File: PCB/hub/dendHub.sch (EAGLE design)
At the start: 12 parts

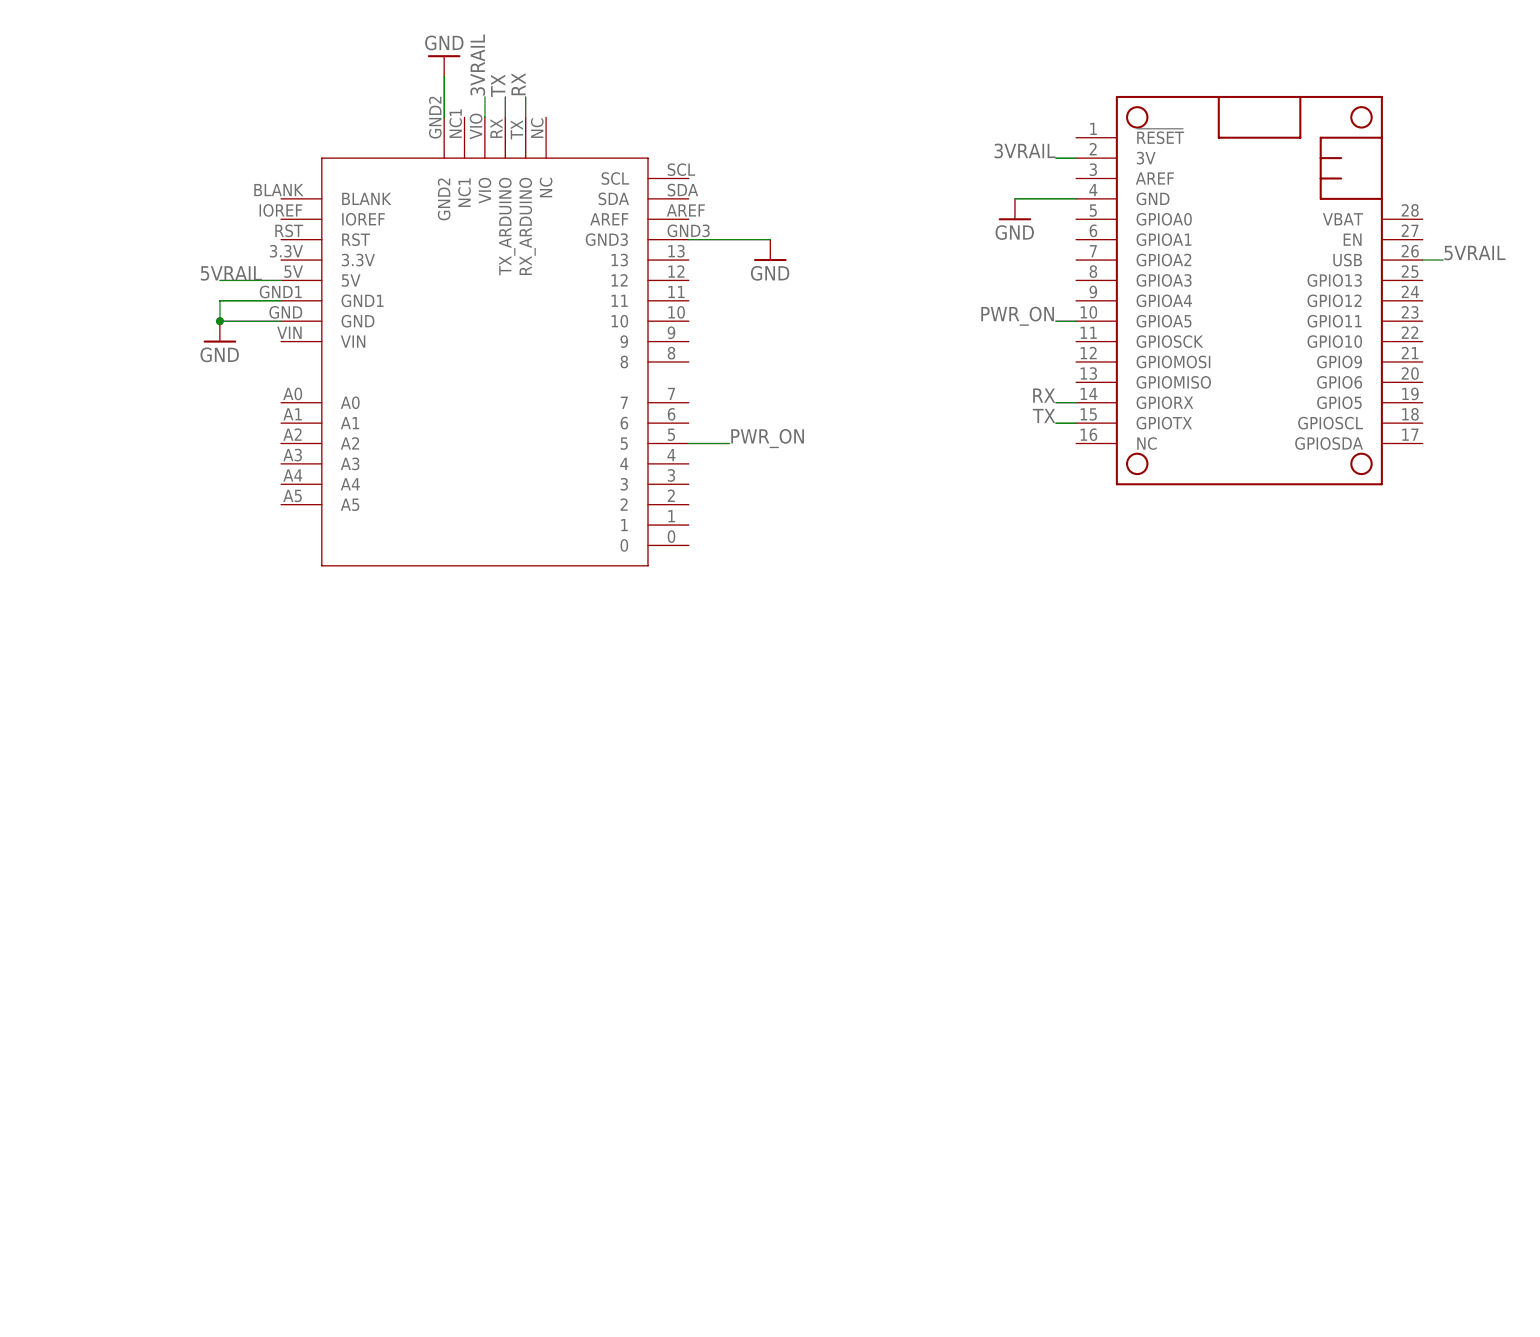
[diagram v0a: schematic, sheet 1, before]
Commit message: Summer 2022 Deployment Prep
Updated PCBs and code, includes Loom V3 and HypnosV3.3 changes
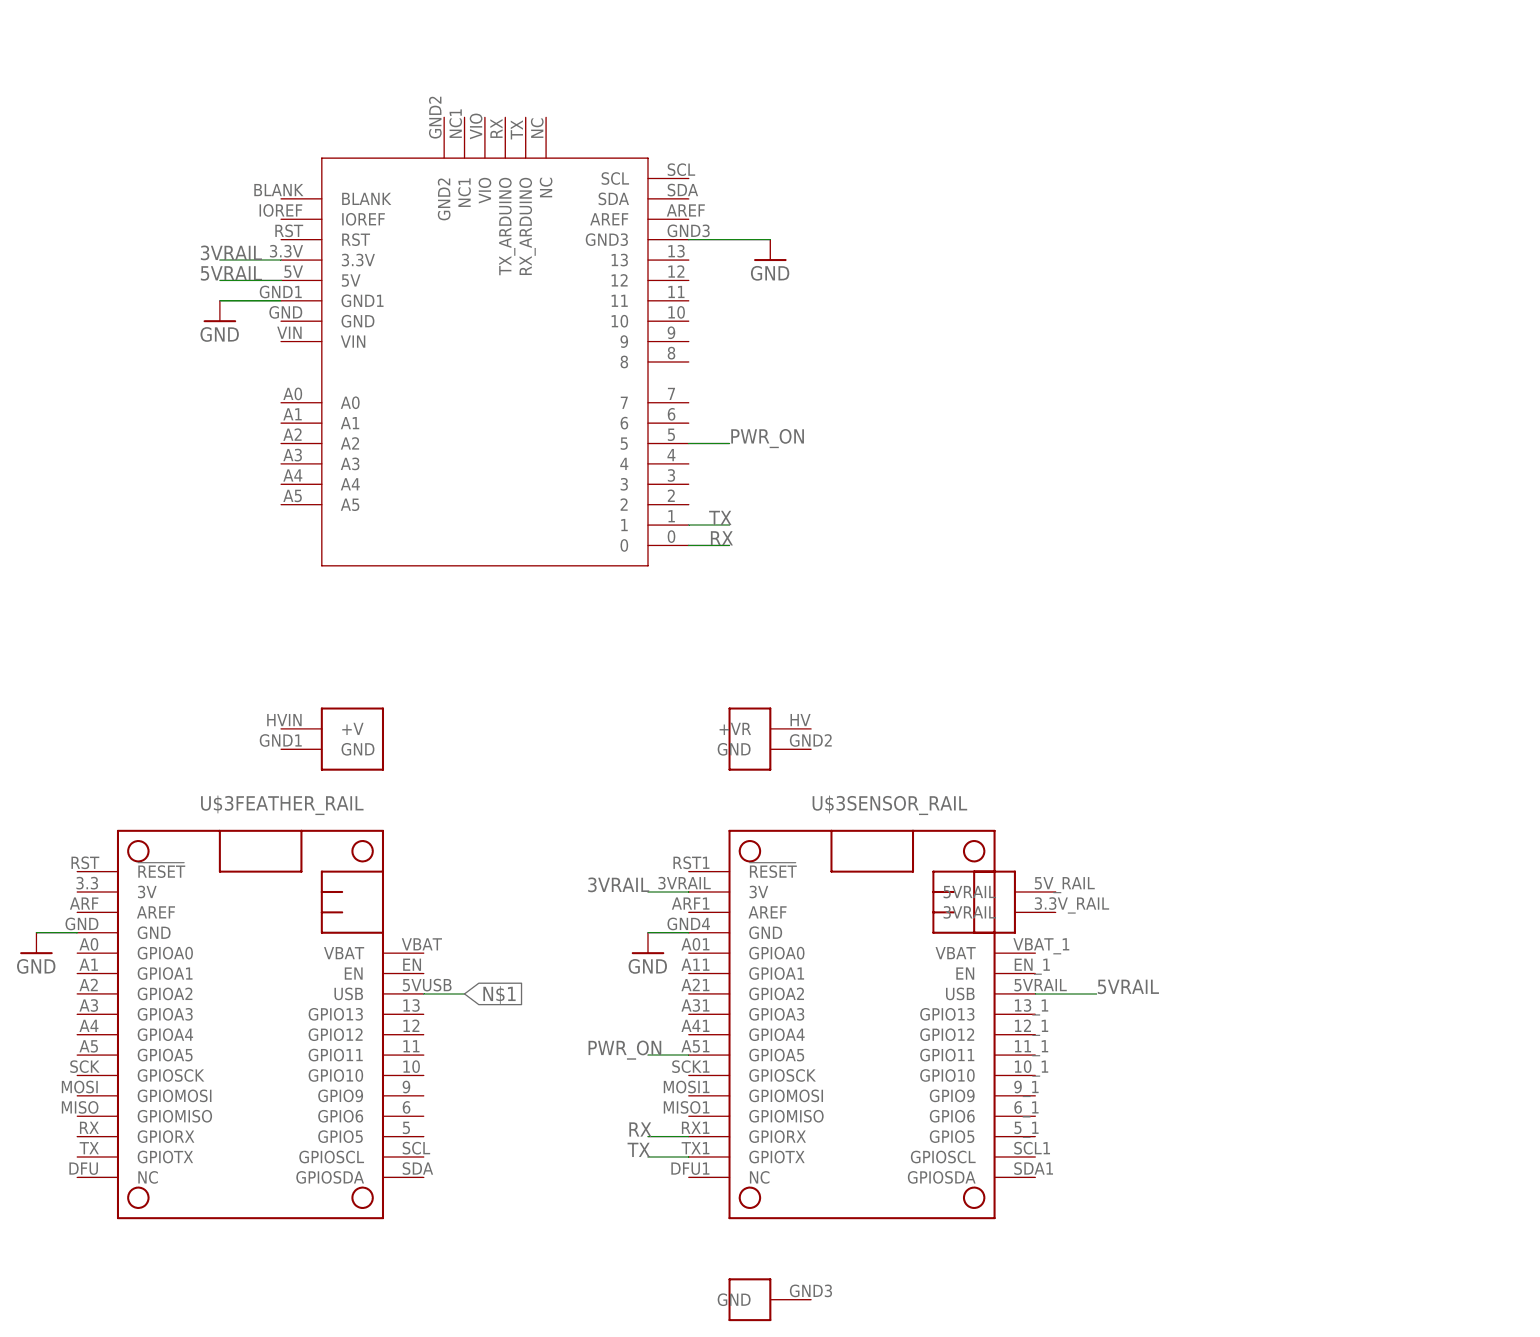
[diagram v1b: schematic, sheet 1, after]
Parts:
- removed MS1: FEATHERWING, adafruit:FEATHERWING
- added U$3: HYPNOS_V3, HYPNOS_V3:HYPNOS_V3
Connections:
- net 3VRAIL: now also U$1.3.3V, U$3SENSOR_RAIL.3V; no longer MS1.3V, U$1.VIO
- net 5VRAIL: now also U$3SENSOR_RAIL.USB; no longer MS1.USB
- net GND: now also U$3FEATHER_RAIL.GND, U$3SENSOR_RAIL.GND; no longer MS1.GND, U$1.GND, U$1.GND2
- net N$1: now also U$3FEATHER_RAIL.USB
- net PWR_ON: now also U$3SENSOR_RAIL.GPIOA5; no longer MS1.GPIOA5
- net RX: now also U$1.0, U$3SENSOR_RAIL.GPIORX; no longer MS1.GPIORX, U$1.RX_ARDUINO
- net TX: now also U$1.1, U$3SENSOR_RAIL.GPIOTX; no longer MS1.GPIOTX, U$1.TX_ARDUINO
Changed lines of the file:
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@@
 <groups>
 <schematic_group name="LTE_BOARD"/>
-<schematic_group name="FEATHER"/>
 <schematic_group name="SOLARCHARGER"/>
 <schematic_group name="POWERBOOSTER"/>
+<schematic_group name="FEATHER/HYPNOS"/>
 </groups>
 <parts>
-<part name="GND1" library="supply1" library_urn="urn:adsk.eagle:library:371" deviceset="GND" device=""/>
-<part name="MS1" library="adafruit" deviceset="FEATHERWING" device="" package3d_urn="urn:adsk.eagle:package:6240959/1"/>
 <part name="U$1" library="LTE_BOARD" deviceset="LTE_BOARD" device=""/>
-<part name="GND5" library="supply1" library_urn="urn:adsk.eagle:library:371" deviceset="GND" device=""/>
 <part name="GND9" library="supply1" library_urn="urn:adsk.eagle:library:371" deviceset="GND" device=""/>
 <part name="GND6" library="supply1" library_urn="urn:adsk.eagle:library:371" deviceset="GND" device=""/>
@@
 <part name="U$83" library="microbuilder" deviceset="GND" device=""/>
 <part name="JP1" library="microbuilder" deviceset="HEADER-1X8" device="ROUND"/>
+<part name="U$3" library="HYPNOS_V3" deviceset="HYPNOS_V3" device="" package3d_urn="urn:adsk.eagle:package:28031607/1"/>
+<part name="GND2" library="supply1" library_urn="urn:adsk.eagle:library:371" deviceset="GND" device=""/>
+<part name="GND3" library="supply1" library_urn="urn:adsk.eagle:library:371" deviceset="GND" device=""/>
 </parts>
 <sheets>
@@
 </plain>
 <instances>
-<instance part="GND1" gate="1" x="-81.28" y="198.12" smashed="yes" grouprefs="FEATHER">
-<attribute name="VALUE" x="-83.82" y="195.58" size="1.778" layer="96"/>
-</instance>
-<instance part="MS1" gate="G$1" x="-68.58" y="213.36" smashed="yes" rot="R270" grouprefs="FEATHER"/>
 <instance part="U$1" gate="G$1" x="-157.48" y="177.8" smashed="yes" grouprefs="LTE_BOARD"/>
-<instance part="GND5" gate="1" x="-152.4" y="218.44" smashed="yes" rot="R180" grouprefs="LTE_BOARD">
-<attribute name="VALUE" x="-149.86" y="220.98" size="1.778" layer="96" rot="R180"/>
-</instance>
 <instance part="GND9" gate="1" x="-111.76" y="193.04" smashed="yes" grouprefs="LTE_BOARD">
 <attribute name="VALUE" x="-114.3" y="190.5" size="1.778" layer="96"/>
 </instance>
-<instance part="GND6" gate="1" x="-180.34" y="182.88" smashed="yes" grouprefs="LTE_BOARD">
-<attribute name="VALUE" x="-182.88" y="180.34" size="1.778" layer="96"/>
+<instance part="GND6" gate="1" x="-180.34" y="185.42" smashed="yes" grouprefs="LTE_BOARD">
+<attribute name="VALUE" x="-182.88" y="182.88" size="1.778" layer="96"/>
+</instance>
+<instance part="U$3" gate="FEATHER_RAIL" x="-195.58" y="81.28" smashed="yes" grouprefs="FEATHER/HYPNOS">
+<attribute name="NAME" x="-182.88" y="124.46" size="1.778" layer="95"/>
+</instance>
+<instance part="U$3" gate="SENSOR_RAIL" x="-119.38" y="81.28" smashed="yes" grouprefs="FEATHER/HYPNOS">
+<attribute name="NAME" x="-106.68" y="124.46" size="1.778" layer="95"/>
+</instance>
+<instance part="U$3" gate="G$1" x="-215.9" y="91.44" smashed="yes" grouprefs="FEATHER/HYPNOS"/>
+<instance part="U$3" gate="G$2" x="-114.3" y="132.08" smashed="yes" grouprefs="FEATHER/HYPNOS"/>
+<instance part="U$3" gate="G$3" x="-114.3" y="63.5" smashed="yes" grouprefs="FEATHER/HYPNOS"/>
+<instance part="U$3" gate="G$4" x="-83.82" y="111.76" smashed="yes" grouprefs="FEATHER/HYPNOS"/>
+<instance part="GND2" gate="1" x="-203.2" y="106.68" smashed="yes" grouprefs="FEATHER/HYPNOS">
+<attribute name="VALUE" x="-205.74" y="104.14" size="1.778" layer="96"/>
+</instance>
+<instance part="GND3" gate="1" x="-127" y="106.68" smashed="yes" grouprefs="FEATHER/HYPNOS">
+<attribute name="VALUE" x="-129.54" y="104.14" size="1.778" layer="96"/>
 </instance>
 </instances>
@@
 <nets>
 <net name="GND" class="0">
-<segment>
-<pinref part="GND1" gate="1" pin="GND"/>
-<wire x1="-81.28" y1="200.66" x2="-73.66" y2="200.66" width="0.1524" layer="91" grouprefs="FEATHER"/>
-<pinref part="MS1" gate="G$1" pin="GND"/>
-</segment>
-<segment>
-<wire x1="-152.4" y1="210.82" x2="-152.4" y2="215.9" width="0.1524" layer="91" grouprefs="LTE_BOARD"/>
-<pinref part="U$1" gate="G$1" pin="GND2"/>
-<pinref part="GND5" gate="1" pin="GND"/>
-</segment>
 <segment>
 <pinref part="U$1" gate="G$1" pin="GND3"/>
@@
 <pinref part="U$1" gate="G$1" pin="GND1"/>
 <wire x1="-172.72" y1="187.96" x2="-180.34" y2="187.96" width="0.1524" layer="91" grouprefs="LTE_BOARD"/>
-<wire x1="-180.34" y1="187.96" x2="-180.34" y2="185.42" width="0.1524" layer="91" grouprefs="LTE_BOARD"/>
-<pinref part="U$1" gate="G$1" pin="GND"/>
-<wire x1="-180.34" y1="185.42" x2="-172.72" y2="185.42" width="0.1524" layer="91" grouprefs="LTE_BOARD"/>
 <pinref part="GND6" gate="1" pin="GND"/>
-<junction x="-180.34" y="185.42" grouprefs="LTE_BOARD"/>
+</segment>
+<segment>
+<pinref part="U$3" gate="FEATHER_RAIL" pin="GND"/>
+<wire x1="-198.12" y1="109.22" x2="-203.2" y2="109.22" width="0.1524" layer="91" grouprefs="FEATHER/HYPNOS"/>
+<pinref part="GND2" gate="1" pin="GND"/>
+</segment>
+<segment>
+<pinref part="U$3" gate="SENSOR_RAIL" pin="GND"/>
+<wire x1="-121.92" y1="109.22" x2="-127" y2="109.22" width="0.1524" layer="91" grouprefs="FEATHER/HYPNOS"/>
+<pinref part="GND3" gate="1" pin="GND"/>
 </segment>
 </net>
 <net name="TX" class="0">
 <segment>
-<wire x1="-73.66" y1="172.72" x2="-76.2" y2="172.72" width="0.1524" layer="91" grouprefs="FEATHER"/>
-<label x="-76.2" y="172.72" size="1.778" layer="95" rot="MR0" grouprefs="FEATHER"/>
-<pinref part="MS1" gate="G$1" pin="GPIOTX"/>
+<pinref part="U$1" gate="G$1" pin="1"/>
+<wire x1="-121.92" y1="160.02" x2="-116.84" y2="160.02" width="0.1524" layer="91"/>
+<label x="-119.38" y="160.02" size="1.778" layer="95"/>
 </segment>
 <segment>
-<wire x1="-144.78" y1="210.82" x2="-144.78" y2="213.36" width="0.1524" layer="91" grouprefs="LTE_BOARD"/>
-<label x="-144.78" y="213.36" size="1.778" layer="95" rot="R90" grouprefs="LTE_BOARD"/>
-<pinref part="U$1" gate="G$1" pin="TX_ARDUINO"/>
+<pinref part="U$3" gate="SENSOR_RAIL" pin="GPIOTX"/>
+<wire x1="-121.92" y1="81.28" x2="-127" y2="81.28" width="0.1524" layer="91" grouprefs="FEATHER/HYPNOS"/>
+<label x="-129.54" y="81.28" size="1.778" layer="95" grouprefs="FEATHER/HYPNOS"/>
 </segment>
 </net>
 <net name="RX" class="0">
 <segment>
-<wire x1="-73.66" y1="175.26" x2="-76.2" y2="175.26" width="0.1524" layer="91" grouprefs="FEATHER"/>
-<label x="-76.2" y="175.26" size="1.778" layer="95" rot="MR0" grouprefs="FEATHER"/>
-<pinref part="MS1" gate="G$1" pin="GPIORX"/>
+<pinref part="U$1" gate="G$1" pin="0"/>
+<wire x1="-121.92" y1="157.48" x2="-116.84" y2="157.48" width="0.1524" layer="91"/>
+<label x="-119.38" y="157.48" size="1.778" layer="95"/>
 </segment>
 <segment>
-<wire x1="-142.24" y1="210.82" x2="-142.24" y2="213.36" width="0.1524" layer="91" grouprefs="LTE_BOARD"/>
-<label x="-142.24" y="213.36" size="1.778" layer="95" rot="R90" grouprefs="LTE_BOARD"/>
-<pinref part="U$1" gate="G$1" pin="RX_ARDUINO"/>
+<pinref part="U$3" gate="SENSOR_RAIL" pin="GPIORX"/>
+<wire x1="-121.92" y1="83.82" x2="-127" y2="83.82" width="0.1524" layer="91" grouprefs="FEATHER/HYPNOS"/>
+<label x="-129.54" y="83.82" size="1.778" layer="95" grouprefs="FEATHER/HYPNOS"/>
 </segment>
 </net>
@@
 </segment>
 <segment>
-<wire x1="-73.66" y1="185.42" x2="-76.2" y2="185.42" width="0.1524" layer="91" grouprefs="FEATHER"/>
-<label x="-76.2" y="185.42" size="1.778" layer="95" rot="MR0" grouprefs="FEATHER"/>
-<pinref part="MS1" gate="G$1" pin="GPIOA5"/>
+<pinref part="U$3" gate="SENSOR_RAIL" pin="GPIOA5"/>
+<wire x1="-121.92" y1="93.98" x2="-127" y2="93.98" width="0.1524" layer="91" grouprefs="FEATHER/HYPNOS"/>
+<label x="-134.62" y="93.98" size="1.778" layer="95" grouprefs="FEATHER/HYPNOS"/>
 </segment>
 </net>
 <net name="5VRAIL" class="0">
-<segment>
-<wire x1="-30.48" y1="193.04" x2="-27.94" y2="193.04" width="0.1524" layer="91" grouprefs="FEATHER"/>
-<label x="-27.94" y="193.04" size="1.778" layer="95" grouprefs="FEATHER"/>
-<pinref part="MS1" gate="G$1" pin="USB"/>
-</segment>
 <segment>
 <pinref part="U$1" gate="G$1" pin="5V"/>
@@
 <label x="-182.88" y="190.5" size="1.778" layer="95" grouprefs="LTE_BOARD"/>
 </segment>
+<segment>
+<pinref part="U$3" gate="SENSOR_RAIL" pin="USB"/>
+<wire x1="-78.74" y1="101.6" x2="-71.12" y2="101.6" width="0.1524" layer="91" grouprefs="FEATHER/HYPNOS"/>
+<label x="-71.12" y="101.6" size="1.778" layer="95" grouprefs="FEATHER/HYPNOS"/>
+</segment>
 </net>
 <net name="3VRAIL" class="0">
 <segment>
-<wire x1="-147.32" y1="210.82" x2="-147.32" y2="213.36" width="0.1524" layer="91" grouprefs="LTE_BOARD"/>
-<label x="-147.32" y="213.36" size="1.778" layer="95" rot="R90" grouprefs="LTE_BOARD"/>
-<pinref part="U$1" gate="G$1" pin="VIO"/>
+<pinref part="U$1" gate="G$1" pin="3.3V"/>
+<wire x1="-172.72" y1="193.04" x2="-180.34" y2="193.04" width="0.1524" layer="91"/>
+<label x="-182.88" y="193.04" size="1.778" layer="95"/>
 </segment>
 <segment>
-<wire x1="-76.2" y1="205.74" x2="-73.66" y2="205.74" width="0.1524" layer="91" grouprefs="FEATHER"/>
-<label x="-76.2" y="205.74" size="1.778" layer="95" rot="MR0" grouprefs="FEATHER"/>
-<pinref part="MS1" gate="G$1" pin="3V"/>
+<pinref part="U$3" gate="SENSOR_RAIL" pin="3V"/>
+<wire x1="-121.92" y1="114.3" x2="-127" y2="114.3" width="0.1524" layer="91"/>
+<label x="-134.62" y="114.3" size="1.778" layer="95"/>
 </segment>
 </net>
+<net name="N$1" class="0">
+<segment>
+<pinref part="U$3" gate="FEATHER_RAIL" pin="USB"/>
+<wire x1="-154.94" y1="101.6" x2="-149.86" y2="101.6" width="0.1524" layer="91" grouprefs="FEATHER/HYPNOS"/>
+<label x="-149.86" y="101.6" size="1.778" layer="95" xref="yes" grouprefs="FEATHER/HYPNOS"/>
+</segment>
+</net>
